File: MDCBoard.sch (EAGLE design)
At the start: 201 parts, among them J1 JUMPER-SOLDER, J10 USB-C-RECEPTACLE-KOREANHRO, J2 JUMPER-SOLDER, J3 JUMPER-SOLDER, J4 JUMPER-SOLDER, J5 BATTERY-HEADER-MOLEX-781710002, J6 JUMPER-SOLDER, J7 JUMPER-SOLDER, J8 JUMPER-SOLDER, J9 MICROSD-SOCKET, Q1 PMOS-NEXPERIA-SOT1220, Q2 PMOS-NEXPERIA-SOT1220, Q3 PMOS-NEXPERIA-SOT1220, Q6 DIODESINC-DMG2305UX, Q7 DIODESINC-DMG2305UX, Q8 DIODESINC-DMG2305UX, SW1 TACTILE-SWITCH, U1 TI-TPS2116, U10 TI-TPS22919DCK, U11 TI-TPS22919DCK, U12 TI-TPS22919DCK, U13 TI-TPS22919DCK, U14 TI-MSP430FR2433IRGE, U15 TI-TXB0102, U16 PANASONIC-EKMB110711X, U17 LATTICE-ICE40HX4K-BG121, U18 WINBOND-W25Q40EW, U19 NEXPERIA-74LVC1G98-OR-INV-INP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, U2 DIODESINC-AP7350, U20 NEXPERIA-74LVC1G98-BUFFER, U21 ON-AR0330CS1C12SPKA0, U22 ALLIANCE-AS4C8M16MSA-6BIN, U23 NEXPERIA-74LVC1G98-INVERTER, U24 STM-STM32F730, U25 DIODESINC-DT1446-04V-7, U26 NEXPERIA-74LVC1G98-MUX-INV-OU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, U27 NEXPERIA-74LVC1G98-MUX-INV-OU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, U28 TI-TPS22919DCK, U3 NEXPERIA-74LVC1G98-NOR, U4 MICROCHIP-MCP7383X, U6 EATON-STN101, U7 TI-TPS62A01, U8 TI-TPS62A01, U9 TI-TPS62A01, X1 EPSON-FC-135, X2 SITIME-SIT8021, X3 SITIME-SIT8021

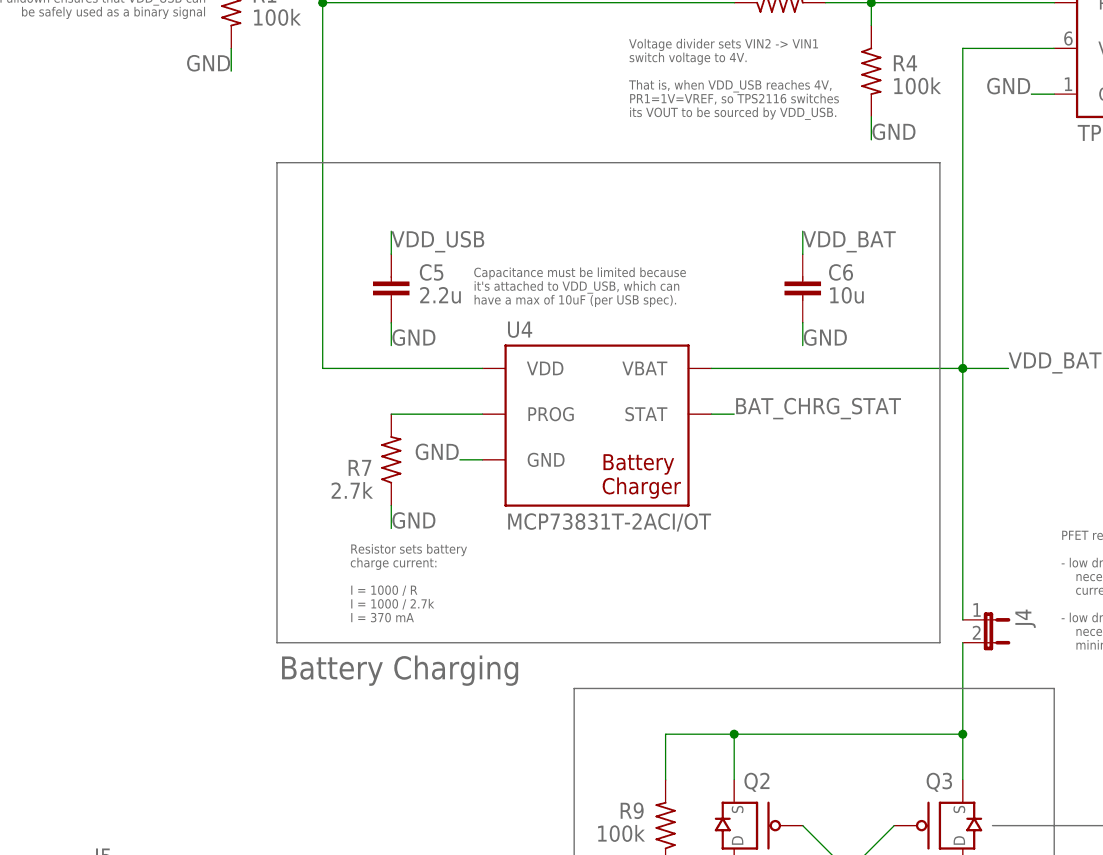
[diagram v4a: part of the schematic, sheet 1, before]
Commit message: Connect ground of R7 to a 5-V tolerant GPIO of STM32
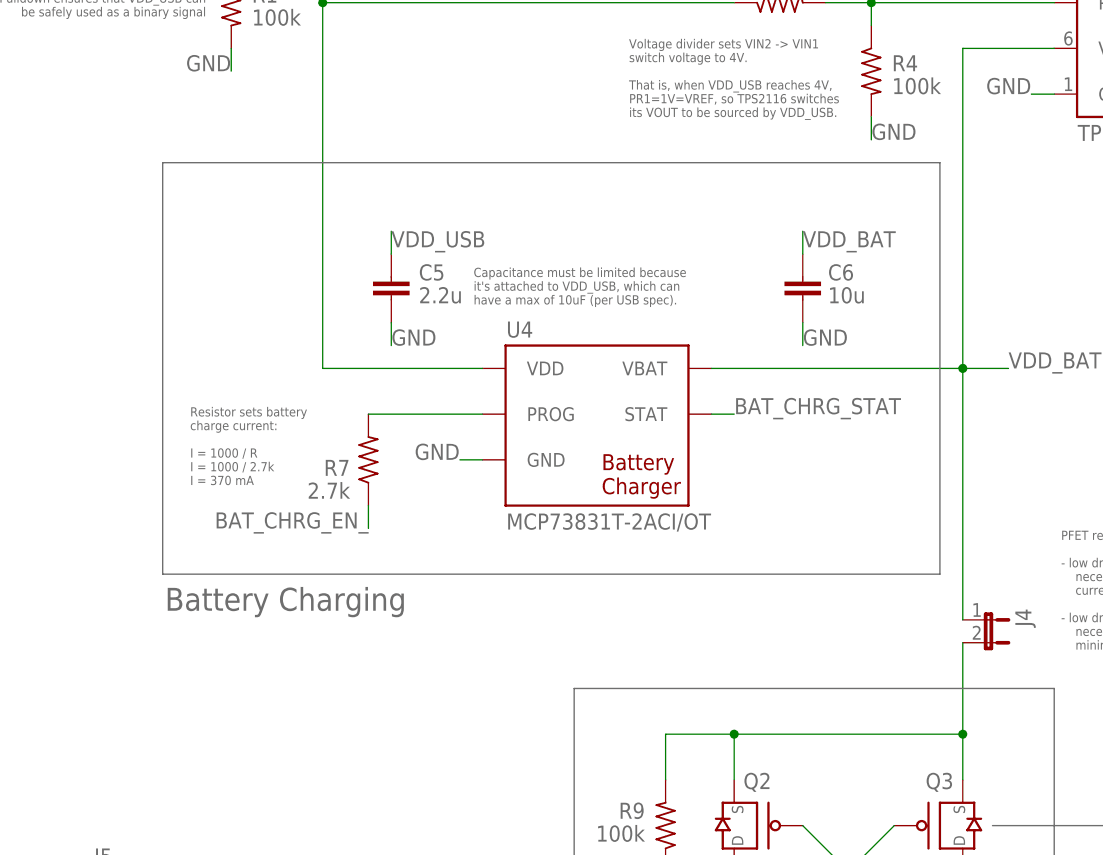
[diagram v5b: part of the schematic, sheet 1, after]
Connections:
- new net BAT_CHRG_EN_: R7.1, U24E.PE14_P11
- net GND: no longer R7.1
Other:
- moved on the sheet: R7
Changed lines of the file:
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@@
 <wire x1="231.14" y1="375.92" x2="177.8" y2="375.92" width="0.1524" layer="95"/>
 <text x="180.594" y="333.756" size="2.54" layer="95" align="top-left">Battery reverse polarity protection</text>
-<text x="152.908" y="391.922" size="1.016" layer="95" align="top-left">Resistor sets battery
+<text x="135.128" y="407.162" size="1.016" layer="95" align="top-left">Resistor sets battery
 charge current:
 I = 1000 / R
@@
 <wire x1="426.72" y1="381" x2="256.54" y2="381" width="0.1524" layer="95"/>
 <text x="259.334" y="323.596" size="2.54" layer="95" align="top-left">Battery Charge Level</text>
-<wire x1="144.78" y1="434.34" x2="144.78" y2="381" width="0.1524" layer="95"/>
-<wire x1="144.78" y1="381" x2="218.44" y2="381" width="0.1524" layer="95"/>
-<wire x1="218.44" y1="381" x2="218.44" y2="434.34" width="0.1524" layer="95"/>
-<wire x1="218.44" y1="434.34" x2="144.78" y2="434.34" width="0.1524" layer="95"/>
-<text x="145.034" y="379.476" size="2.54" layer="95" align="top-left">Battery Charging</text>
+<wire x1="132.08" y1="434.34" x2="132.08" y2="388.62" width="0.1524" layer="95"/>
+<wire x1="132.08" y1="388.62" x2="218.44" y2="388.62" width="0.1524" layer="95"/>
+<wire x1="218.44" y1="388.62" x2="218.44" y2="434.34" width="0.1524" layer="95"/>
+<wire x1="218.44" y1="434.34" x2="132.08" y2="434.34" width="0.1524" layer="95"/>
+<text x="132.334" y="387.096" size="2.54" layer="95" align="top-left">Battery Charging</text>
 <text x="260.35" y="346.71" size="1.524" layer="95" align="top-left">This subcircuit divides VDD_BAT by 1.33, and also prevents
 the battery drain caused by the voltage divider unless
@@
 <attribute name="PN" x="170.255" y="393.5759" size="1.778" layer="95" ratio="10" rot="SR0"/>
 </instance>
-<instance part="R7" gate="G$1" x="157.48" y="401.32" smashed="yes" rot="R90">
-<attribute name="NAME" x="155.448" y="401.32" size="1.778" layer="95" align="top-right"/>
-<attribute name="VALUE" x="155.448" y="398.78" size="1.778" layer="96" align="top-right"/>
-<attribute name="MFG" x="157.48" y="401.32" size="1.778" layer="96" rot="R90" display="off"/>
-<attribute name="PN" x="157.48" y="401.32" size="1.778" layer="96" rot="R90" display="off"/>
+<instance part="R7" gate="G$1" x="154.94" y="401.32" smashed="yes" rot="R90">
+<attribute name="NAME" x="152.908" y="401.32" size="1.778" layer="95" align="top-right"/>
+<attribute name="VALUE" x="152.908" y="398.78" size="1.778" layer="96" align="top-right"/>
+<attribute name="MFG" x="154.94" y="401.32" size="1.778" layer="96" rot="R90" display="off"/>
+<attribute name="PN" x="154.94" y="401.32" size="1.778" layer="96" rot="R90" display="off"/>
 </instance>
 <instance part="Q3" gate="G$1" x="220.98" y="355.6" smashed="yes" rot="R90">
@@
 </segment>
 <segment>
-<pinref part="R7" gate="G$1" pin="1"/>
-<wire x1="157.48" y1="396.24" x2="157.48" y2="393.7" width="0.1524" layer="91"/>
-<label x="157.48" y="393.7" size="1.778" layer="95"/>
-</segment>
-<segment>
 <pinref part="R12" gate="G$1" pin="2"/>
 <wire x1="220.98" y1="340.36" x2="220.98" y2="337.82" width="0.1524" layer="91"/>
@@
 <pinref part="R7" gate="G$1" pin="2"/>
 <pinref part="U4" gate="G$1" pin="PROG"/>
-<wire x1="157.48" y1="406.4" x2="167.64" y2="406.4" width="0.1524" layer="91"/>
+<wire x1="154.94" y1="406.4" x2="167.64" y2="406.4" width="0.1524" layer="91"/>
 </segment>
 </net>
@@
 </segment>
 </net>
+<net name="BAT_CHRG_EN_" class="0">
+<segment>
+<pinref part="R7" gate="G$1" pin="1"/>
+<wire x1="154.94" y1="396.24" x2="154.94" y2="393.7" width="0.1524" layer="91"/>
+<label x="154.94" y="393.7" size="1.778" layer="95" align="bottom-right"/>
+</segment>
+</net>
 </nets>
 </sheet>
@@
 </segment>
 </net>
+<net name="BAT_CHRG_EN_" class="0">
+<segment>
+<pinref part="U24" gate="E" pin="PE14_P11"/>
+<wire x1="2.54" y1="-109.22" x2="5.08" y2="-109.22" width="0.1524" layer="91"/>
+<label x="5.08" y="-109.22" size="1.778" layer="95"/>
+</segment>
+</net>

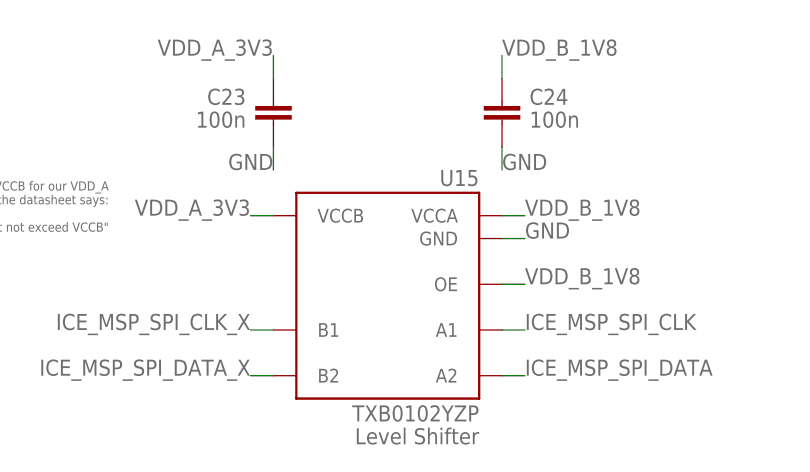
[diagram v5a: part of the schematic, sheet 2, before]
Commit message: - Switch ICE<->MSP level shifter to NXB0102UN (BGA)
- Move C19 a bit further away from SD card holder
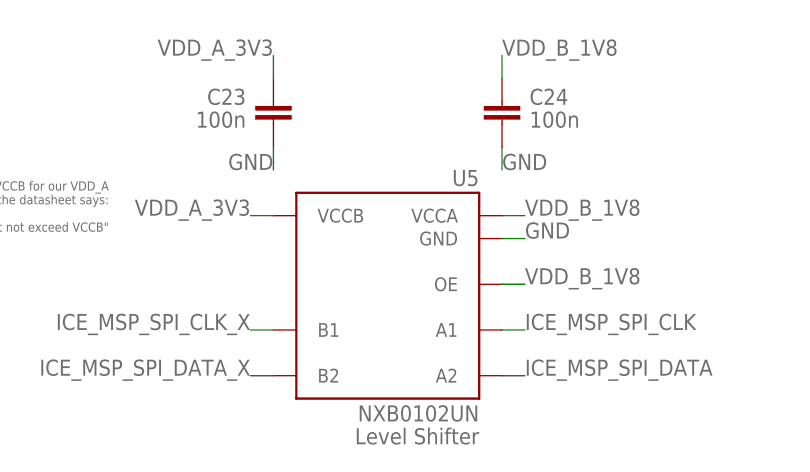
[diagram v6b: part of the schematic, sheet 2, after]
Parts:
- removed U15: TI-TXB0102, EagleLibrary:TI-TXB0102
- added U5: NEXPERIA-NXB0102, EagleLibrary:NEXPERIA-NXB0102
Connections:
- net GND: now also U5.GND; no longer U15.GND
- net ICE_MSP_SPI_CLK: now also U5.A1; no longer U15.A1
- net ICE_MSP_SPI_CLK_X: now also U5.B1; no longer U15.B1
- net ICE_MSP_SPI_DATA: now also U5.A2; no longer U15.A2
- net ICE_MSP_SPI_DATA_X: now also U5.B2; no longer U15.B2
- net VDD_A_3V3: now also U5.VCCB; no longer U15.VCCB
- net VDD_B_1V8: now also U5.OE, U5.VCCA; no longer U15.OE, U15.VCCA
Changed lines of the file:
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@@
 <attribute name="PN" value="GRM155R61H104KE19D"/>
 </part>
-<part name="U15" library="EagleLibrary" deviceset="TI-TXB0102" device=""/>
 <part name="Q1" library="EagleLibrary" deviceset="PMOS" device="-NEXPERIA-SOT1220">
 <attribute name="PN" value="PMPB10UPX"/>
@@
 <part name="U27" library="EagleLibrary" deviceset="NEXPERIA-74LVC1G98-MUX-INV-OUTPUT" device=""/>
 <part name="U28" library="EagleLibrary" deviceset="TI-TPS22919DCK" device=""/>
+<part name="U5" library="EagleLibrary" deviceset="NEXPERIA-NXB0102" device=""/>
 </parts>
 <sheets>
@@
 <attribute name="VALUE" x="45.974" y="93.599" size="1.778" layer="96"/>
 </instance>
-<instance part="U15" gate="G$1" x="76.2" y="25.4" smashed="yes" rot="MR0">
-<attribute name="PN" x="76.2" y="0" size="1.778" layer="95" rot="MR0"/>
-<attribute name="NAME" x="76.2" y="27.94" size="1.778" layer="95" rot="MR0" align="top-left"/>
-</instance>
 <instance part="X1" gate="G$1" x="254" y="104.14" smashed="yes" rot="MR0">
 <attribute name="NAME" x="254" y="106.426" size="1.778" layer="95" rot="MR0" align="top-left"/>
@@
 <attribute name="PN" x="345.44" y="75.438" size="1.778" layer="95" align="top-left"/>
 </instance>
+<instance part="U5" gate="G$1" x="76.2" y="25.4" smashed="yes" rot="MR0">
+<attribute name="PN" x="76.2" y="0" size="1.778" layer="95" rot="MR0"/>
+<attribute name="NAME" x="76.2" y="27.94" size="1.778" layer="95" rot="MR0" align="top-left"/>
+</instance>
 </instances>
 <busses>
@@
 </segment>
 <segment>
-<pinref part="U15" gate="G$1" pin="VCCB"/>
 <wire x1="53.34" y1="22.86" x2="50.8" y2="22.86" width="0.1524" layer="91"/>
 <label x="50.8" y="22.86" size="1.778" layer="95" rot="MR0"/>
+<pinref part="U5" gate="G$1" pin="VCCB"/>
 </segment>
 <segment>
@@
 </segment>
 <segment>
-<pinref part="U15" gate="G$1" pin="GND"/>
 <wire x1="78.74" y1="20.32" x2="81.28" y2="20.32" width="0.1524" layer="91"/>
 <label x="81.28" y="20.32" size="1.778" layer="95" rot="MR0" align="bottom-right"/>
+<pinref part="U5" gate="G$1" pin="GND"/>
 </segment>
 <segment>
@@
 <wire x1="53.34" y1="5.08" x2="50.8" y2="5.08" width="0.1524" layer="91"/>
 <label x="50.8" y="5.08" size="1.778" layer="95" align="bottom-right"/>
-<pinref part="U15" gate="G$1" pin="B2"/>
+<pinref part="U5" gate="G$1" pin="B2"/>
 </segment>
 <segment>
@@
 <wire x1="53.34" y1="10.16" x2="50.8" y2="10.16" width="0.1524" layer="91"/>
 <label x="50.8" y="10.16" size="1.778" layer="95" align="bottom-right"/>
-<pinref part="U15" gate="G$1" pin="B1"/>
+<pinref part="U5" gate="G$1" pin="B1"/>
 </segment>
 <segment>
@@
 <net name="VDD_B_1V8" class="0">
 <segment>
-<pinref part="U15" gate="G$1" pin="VCCA"/>
 <wire x1="78.74" y1="22.86" x2="81.28" y2="22.86" width="0.1524" layer="91"/>
 <label x="81.28" y="22.86" size="1.778" layer="95"/>
-</segment>
-<segment>
-<pinref part="U15" gate="G$1" pin="OE"/>
+<pinref part="U5" gate="G$1" pin="VCCA"/>
+</segment>
+<segment>
 <wire x1="78.74" y1="15.24" x2="81.28" y2="15.24" width="0.1524" layer="91"/>
 <label x="81.28" y="15.24" size="1.778" layer="95"/>
+<pinref part="U5" gate="G$1" pin="OE"/>
 </segment>
 <segment>
@@
 <wire x1="78.74" y1="10.16" x2="81.28" y2="10.16" width="0.1524" layer="91"/>
 <label x="81.28" y="10.16" size="1.778" layer="95"/>
-<pinref part="U15" gate="G$1" pin="A1"/>
+<pinref part="U5" gate="G$1" pin="A1"/>
 </segment>
 </net>
@@
 <wire x1="78.74" y1="5.08" x2="81.28" y2="5.08" width="0.1524" layer="91"/>
 <label x="81.28" y="5.08" size="1.778" layer="95"/>
-<pinref part="U15" gate="G$1" pin="A2"/>
-</segment>
-</net>
+<pinref part="U5" gate="G$1" pin="A2"/>
+</segment>
+</net>

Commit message: Layout progress
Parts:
- removed LED10, LED9: LEDLED-0603, EagleLibrary:LEDLED-0603
- removed R44, R45: 1k, EagleLibrary:RESISTOR0402
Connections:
- removed net N$27: LED10.C, R45.1
- removed net N$29: LED9.C, R44.1
- removed net STM_LED0: LED10.A, U24B.PB10_R12
- removed net STM_LED1: LED9.A, U24B.PB12_P12
- net BAT_CHRG_EN_: now also U24E.PE15_R11; no longer U24E.PE14_P11
- net BAT_CHRG_STAT: now also U24B.PB10_R12; no longer U24E.PE15_R11
- net GND: no longer R44.2, R45.2
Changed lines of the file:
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@@
 <attribute name="PN" value="SIT8021AI-J4-18S-16.000000E"/>
 </part>
-<part name="LED10" library="EagleLibrary" deviceset="LED" device="LED-0603">
-<attribute name="MFG" value="OSRAM"/>
-<attribute name="PN" value="KS DELLS1.22-JHKI-1"/>
-</part>
-<part name="R45" library="EagleLibrary" deviceset="RESISTOR" device="0402" value="1k">
-<attribute name="MFG" value="Kamaya"/>
-<attribute name="PN" value="RGC1/16SC1001DTH"/>
-</part>
 <part name="R30" library="EagleLibrary" deviceset="RESISTOR" device="0402" value="10k">
 <attribute name="MFG" value="Yageo"/>
@@
 <attribute name="PN" value="RGC1/16SC1001DTH"/>
 </part>
-<part name="LED9" library="EagleLibrary" deviceset="LED" device="LED-0603">
-<attribute name="MFG" value="OSRAM"/>
-<attribute name="PN" value="KS DELLS1.22-JHKI-1"/>
-</part>
-<part name="R44" library="EagleLibrary" deviceset="RESISTOR" device="0402" value="1k">
-<attribute name="MFG" value="Kamaya"/>
-<attribute name="PN" value="RGC1/16SC1001DTH"/>
-</part>
 <part name="LED8" library="EagleLibrary" deviceset="LED" device="LED-0603">
 <attribute name="MFG" value="OSRAM"/>
@@
 <attribute name="PN" x="241.3" y="-30.48" size="1.778" layer="95"/>
 </instance>
-<instance part="LED10" gate="G$1" x="246.38" y="-48.26" smashed="yes">
-<attribute name="NAME" x="249.936" y="-52.832" size="1.778" layer="95" rot="R90"/>
-<attribute name="MFG" x="246.38" y="-48.26" size="1.778" layer="96" display="off"/>
-<attribute name="PN" x="246.38" y="-48.26" size="1.778" layer="96" display="off"/>
-</instance>
-<instance part="R45" gate="G$1" x="246.38" y="-60.96" smashed="yes" rot="R270">
-<attribute name="NAME" x="247.65" y="-58.42" size="1.778" layer="95"/>
-<attribute name="VALUE" x="247.65" y="-60.96" size="1.778" layer="96"/>
-<attribute name="MFG" x="246.38" y="-60.96" size="1.778" layer="96" rot="R270" display="off"/>
-<attribute name="PN" x="246.38" y="-60.96" size="1.778" layer="96" rot="R270" display="off"/>
-</instance>
-<instance part="LED9" gate="G$1" x="231.14" y="-48.26" smashed="yes">
-<attribute name="NAME" x="234.696" y="-52.832" size="1.778" layer="95" rot="R90"/>
-<attribute name="MFG" x="231.14" y="-48.26" size="1.778" layer="96" display="off"/>
-<attribute name="PN" x="231.14" y="-48.26" size="1.778" layer="96" display="off"/>
-</instance>
-<instance part="R44" gate="G$1" x="231.14" y="-60.96" smashed="yes" rot="R270">
-<attribute name="NAME" x="232.41" y="-58.42" size="1.778" layer="95"/>
-<attribute name="VALUE" x="232.41" y="-60.96" size="1.778" layer="96"/>
-<attribute name="MFG" x="231.14" y="-60.96" size="1.778" layer="96" rot="R270" display="off"/>
-<attribute name="PN" x="231.14" y="-60.96" size="1.778" layer="96" rot="R270" display="off"/>
-</instance>
 <instance part="LED8" gate="G$1" x="215.9" y="-48.26" smashed="yes">
 <attribute name="NAME" x="219.456" y="-52.832" size="1.778" layer="95" rot="R90"/>
@@
 </segment>
 <segment>
-<pinref part="R45" gate="G$1" pin="2"/>
-<wire x1="246.38" y1="-66.04" x2="246.38" y2="-68.58" width="0.1524" layer="91"/>
-<label x="246.38" y="-68.58" size="1.778" layer="95"/>
-</segment>
-<segment>
 <pinref part="U24" gate="J" pin="BYPASS_REG_L4"/>
 <wire x1="78.74" y1="-142.24" x2="81.28" y2="-142.24" width="0.1524" layer="91"/>
@@
 </segment>
 <segment>
-<pinref part="R44" gate="G$1" pin="2"/>
-<wire x1="231.14" y1="-66.04" x2="231.14" y2="-68.58" width="0.1524" layer="91"/>
-<label x="231.14" y="-68.58" size="1.778" layer="95"/>
-</segment>
-<segment>
 <pinref part="R43" gate="G$1" pin="2"/>
 <wire x1="215.9" y1="-66.04" x2="215.9" y2="-68.58" width="0.1524" layer="91"/>
@@
 </segment>
 </net>
-<net name="N$27" class="0">
-<segment>
-<pinref part="LED10" gate="G$1" pin="C"/>
-<wire x1="246.38" y1="-53.34" x2="246.38" y2="-55.88" width="0.1524" layer="91"/>
-<pinref part="R45" gate="G$1" pin="1"/>
-</segment>
-</net>
-<net name="STM_LED0" class="0">
-<segment>
-<pinref part="LED10" gate="G$1" pin="A"/>
-<wire x1="246.38" y1="-45.72" x2="246.38" y2="-43.18" width="0.1524" layer="91"/>
-<label x="246.38" y="-43.18" size="1.778" layer="95"/>
-</segment>
-<segment>
-<pinref part="U24" gate="B" pin="PB10_R12"/>
-<wire x1="68.58" y1="-38.1" x2="71.12" y2="-38.1" width="0.1524" layer="91"/>
-<label x="71.12" y="-38.1" size="1.778" layer="95"/>
-</segment>
-</net>
 <net name="VDD_B_3V3_STM" class="0">
 <segment>
@@
 </segment>
 </net>
-<net name="N$29" class="0">
-<segment>
-<pinref part="LED9" gate="G$1" pin="C"/>
-<wire x1="231.14" y1="-53.34" x2="231.14" y2="-55.88" width="0.1524" layer="91"/>
-<pinref part="R44" gate="G$1" pin="1"/>
-</segment>
-</net>
 <net name="N$30" class="0">
 <segment>
@@
 </segment>
 </net>
-<net name="STM_LED1" class="0">
-<segment>
-<pinref part="LED9" gate="G$1" pin="A"/>
-<wire x1="231.14" y1="-45.72" x2="231.14" y2="-43.18" width="0.1524" layer="91"/>
-<label x="231.14" y="-43.18" size="1.778" layer="95"/>
-</segment>
-<segment>
-<pinref part="U24" gate="B" pin="PB12_P12"/>
-<wire x1="68.58" y1="-43.18" x2="71.12" y2="-43.18" width="0.1524" layer="91"/>
-<label x="71.12" y="-43.18" size="1.778" layer="95"/>
-</segment>
-</net>
 <net name="STM_LED2" class="0">
 <segment>
@@
 </segment>
 </net>
-<net name="BAT_CHRG_STAT" class="0">
-<segment>
-<wire x1="2.54" y1="-111.76" x2="5.08" y2="-111.76" width="0.1524" layer="91"/>
-<label x="5.08" y="-111.76" size="1.778" layer="95"/>
-<pinref part="U24" gate="E" pin="PE15_R11"/>
-</segment>
-</net>
 <net name="MSP_STM_I2C_SCL" class="0">
 <segment>
@@
 </segment>
 </net>
+<net name="BAT_CHRG_STAT" class="0">
+<segment>
+<wire x1="68.58" y1="-38.1" x2="71.12" y2="-38.1" width="0.1524" layer="91"/>
+<label x="71.12" y="-38.1" size="1.778" layer="95"/>
+<pinref part="U24" gate="B" pin="PB10_R12"/>
+</segment>
+</net>
 <net name="BAT_CHRG_EN_" class="0">
 <segment>
-<pinref part="U24" gate="E" pin="PE14_P11"/>
-<wire x1="2.54" y1="-109.22" x2="5.08" y2="-109.22" width="0.1524" layer="91"/>
-<label x="5.08" y="-109.22" size="1.778" layer="95"/>
+<wire x1="2.54" y1="-111.76" x2="5.08" y2="-111.76" width="0.1524" layer="91"/>
+<label x="5.08" y="-111.76" size="1.778" layer="95"/>
+<pinref part="U24" gate="E" pin="PE15_R11"/>
 </segment>
 </net>
